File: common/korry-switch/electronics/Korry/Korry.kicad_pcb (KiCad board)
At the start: 2 copper layers, 20.5 x 20.5 mm, 11 parts, among them J1 Conn_01x02_Pin, J2 Conn_01x04_Pin

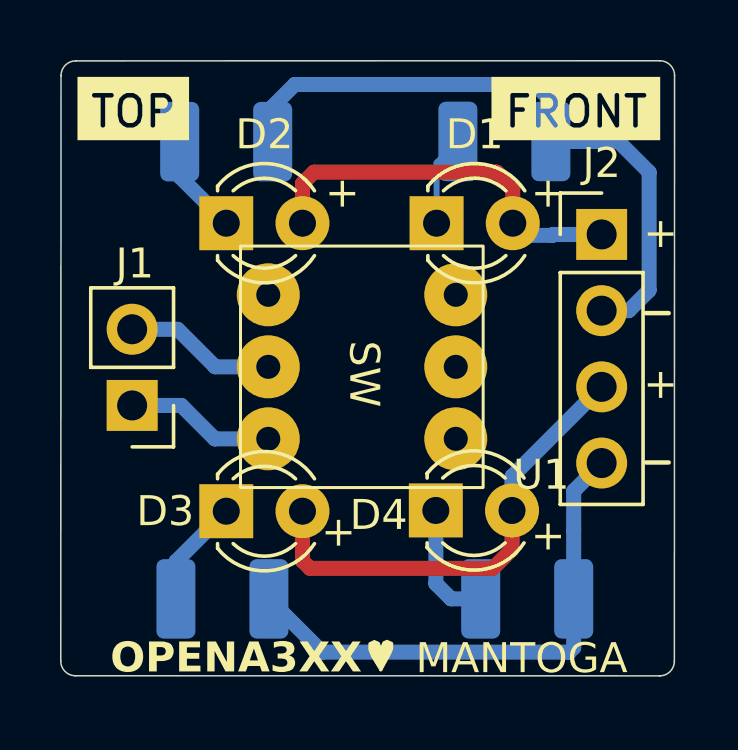
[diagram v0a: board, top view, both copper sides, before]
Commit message: Added KorryPanel + BOM & CPL - COMPLETED
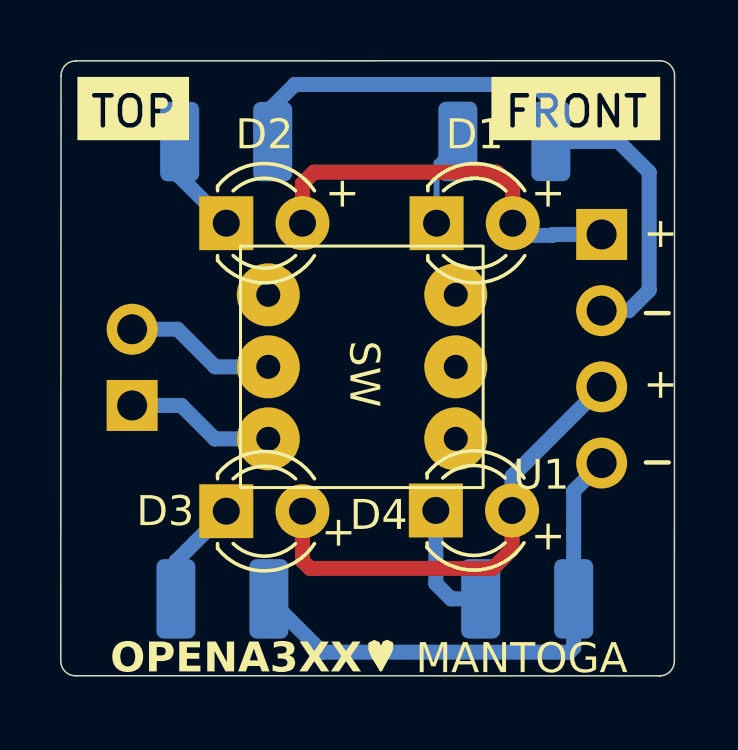
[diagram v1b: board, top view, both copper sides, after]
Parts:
- J1, J2: moved to B.Cu
- turned J1 to 0 degrees
- turned J2 to 180 degrees
